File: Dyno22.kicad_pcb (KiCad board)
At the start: 2 copper layers, 52 parts, among them J1 Pwr Input, J2 Display, J3 Pwr Output, J4 BPM & Sensors, J7 UART, SW1 SW_DPST_x2, U1 TS2937CW50, U2 LM324, U3 74HC4052

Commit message: made some passive components 0805 and changed some routing
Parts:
- added TP5: GND_TestPoint, TestPoint:TestPoint_Loop_D2.60mm_Drill1.4mm_Beaded, F.Cu at (158.8, 128.9)
- D1: value Red -> Red LED
- D2: value LED -> RED LED; footprint LED_SMD:LED_0603_1608Metric -> LED_SMD:LED_0805_2012Metric
- Encoder1: footprint Rotary_Encoder:RotaryEncoder_Alps_EC11E_Vertical_H20mm -> Rotary_Encoder:RotaryEncoder_Alps_EC12E-Switch_Vertical_H20mm_CircularMountingHoles
- R18: value 2.2k -> 1k; footprint Resistor_SMD:R_0402_1005Metric -> Resistor_SMD:R_0805_2012Metric
- R3, R4, R5: value 5kΩ -> 4.7kΩ
- moved TP4 80.0 mm to (124.5, 35.6)
- moved D1 4.02 mm to (188.0, 47.9)
- moved D2 3.49 mm to (191.1, 47.9)
- moved R18 3.02 mm to (194.7, 48.3), turned to 0 degrees
- moved F1 2.54 mm to (200.7, 49.5), turned to 180 degrees
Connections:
- A1 pad 20: /MISO_0 -> /MOSI_1
- F1 pad 1: +24V -> Net-(J1-Pin_2)
- J1 pad 2: +24V -> Net-(J1-Pin_2)
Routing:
- net Net-(D2-K): track 3.34 -> 69.1 mm
- net +24V: track 74.9 -> 12.0 mm
- net Earth: track 41.4 -> 99.1 mm, vias 2 -> 3
- net /ROT_EN_SW: track 47.4 -> 79.8 mm, vias 1 -> 2
- net Net-(D2-A): track 11.3 -> 17.5 mm
- net Net-(D1-A): track 18.1 -> 22.5 mm
- net /BPM_CTRL_OUT: track 68.0 -> 71.3 mm
- net /KILL_SW: track 54.8 -> 53.8 mm
- net /FORCE_IN: track 29.0 -> 29.8 mm

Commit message: Added demux changed LED location changed some Rs
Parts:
- added U3: Demux, KiCADv6:SOIC-16WB_ONS, F.Cu at (173.0, 102.2)
- R3, R4, R5: value 4.7kΩ -> 10kΩ
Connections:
- D2 pad 1: Net-(D2-K) -> Earth
- F1 pad 2: Net-(D2-A) -> Net-(SW1-B)
- R18 pad 1: Net-(D2-K) -> +24V
- R18 pad 2: Earth -> Net-(D2-A)
- SW1 pad 2: Net-(D2-A) -> Net-(SW1-B)
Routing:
- net Net-(D2-K): track 69.1 -> 0.00 mm
- net (no net): track 0.00 -> 69.1 mm

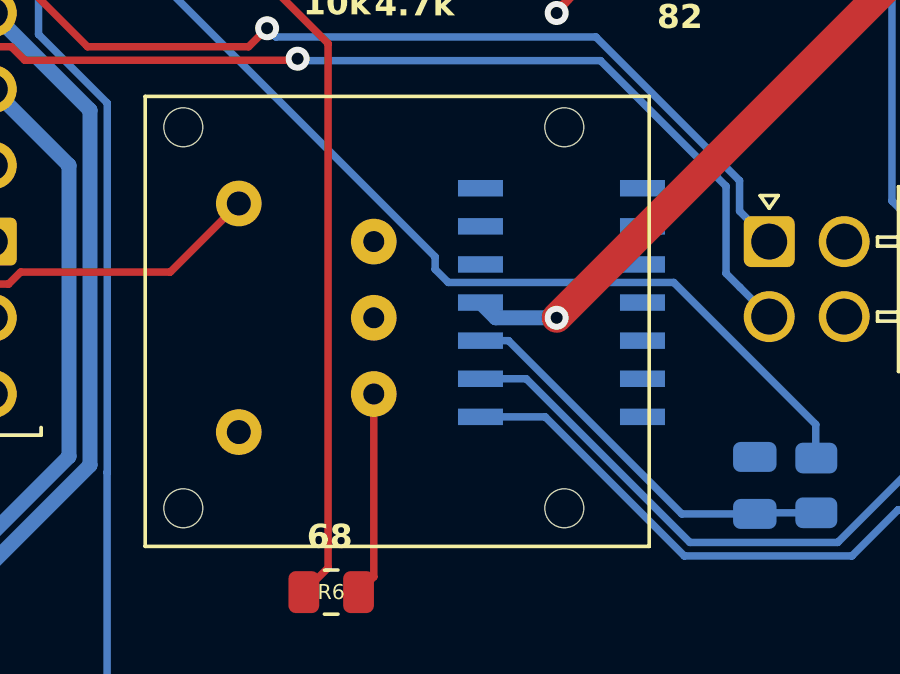
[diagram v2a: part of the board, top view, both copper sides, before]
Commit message: Amplifier footprint changes
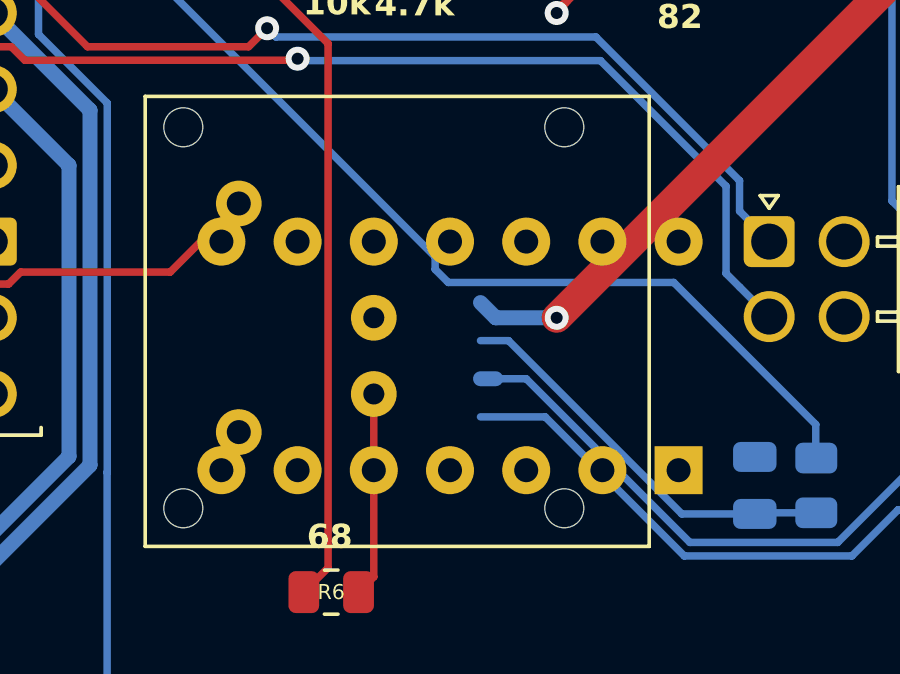
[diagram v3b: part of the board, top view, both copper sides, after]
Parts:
- U2: footprint SOIC:SOIC-14_W3.9mm -> Package_DIP:DIP-14_W7.62mm
- moved U2 6.82 mm to (205.7, 86.4)
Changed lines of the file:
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@@
     )
   )
-  (footprint "SOIC:SOIC-14_W3.9mm" (layer "B.Cu")
-    (at 201.836 80.772 90)
+  (footprint "Package_DIP:DIP-14_W7.62mm" (layer "B.Cu")
+    (at 205.74 86.36 90)
+    (descr "14-lead though-hole mounted DIP package, row spacing 7.62 mm (300 mils)")
+    (tags "THT DIP DIL PDIP 2.54mm 7.62mm 300mil")
     (property "Sheetfile" "Dyno22.kicad_sch")
     (property "Sheetname" "")
     (property "ki_description" "Low Power Single Operational Amplifier, SOT-23-5")
     (property "ki_keywords" "single opamp")
-    (attr smd)
-    (fp_text reference "U2" (at -5.715 0.16) (layer "B.SilkS")
+    (attr through_hole)
+    (fp_text reference "U2" (at 3.81 2.33 270) (layer "B.SilkS")
         (effects (font (size 1 1) (thickness 0.15)) (justify mirror))
     )
-    (fp_text value "LM324" (at 0 -5.29 90) (layer "B.Fab")
+    (fp_text value "LM324" (at 3.81 -17.57 270) (layer "B.Fab")
         (effects (font (size 1 1) (thickness 0.15)) (justify mirror))
     )
-    (fp_text user "REF**" (at 0 0 90) (layer "B.Fab")
+    (fp_text user "${REFERENCE}" (at 3.81 -7.62 270) (layer "B.Fab")
         (effects (font (size 1 1) (thickness 0.15)) (justify mirror))
     )
-    (fp_line (start -4.7 -2.3) (end -4.3 -2.3)
-      (stroke (width 0.1) (type solid)) (layer "B.SilkS"))
-    (fp_line (start -4.7 -1.7) (end -4.7 -2.3)
-      (stroke (width 0.1) (type solid)) (layer "B.SilkS"))
-    (fp_line (start -4.7 2.3) (end -4.7 1.9)
-      (stroke (width 0.1) (type solid)) (layer "B.SilkS"))
-    (fp_line (start -4.3 -2.3) (end -4.3 -3.2)
-      (stroke (width 0.1) (type solid)) (layer "B.SilkS"))
-    (fp_line (start -4.3 2.3) (end -4.7 2.3)
-      (stroke (width 0.1) (type solid)) (layer "B.SilkS"))
-    (fp_line (start 4.3 -2.3) (end 4.6 -2.3)
-      (stroke (width 0.1) (type solid)) (layer "B.SilkS"))
-    (fp_line (start 4.3 2.4) (end 4.7 2.4)
-      (stroke (width 0.1) (type solid)) (layer "B.SilkS"))
-    (fp_line (start 4.6 -2.3) (end 4.6 -1.9)
-      (stroke (width 0.1) (type solid)) (layer "B.SilkS"))
-    (fp_line (start 4.7 2.4) (end 4.7 1.9)
-      (stroke (width 0.1) (type solid)) (layer "B.SilkS"))
-    (fp_line (start -4.65 -3.7) (end -4.65 3.7)
+    (fp_line (start 1.16 -16.57) (end 6.46 -16.57)
+      (stroke (width 0.12) (type solid)) (layer "B.SilkS"))
+    (fp_line (start 1.16 1.33) (end 1.16 -16.57)
+      (stroke (width 0.12) (type solid)) (layer "B.SilkS"))
+    (fp_line (start 2.81 1.33) (end 1.16 1.33)
+      (stroke (width 0.12) (type solid)) (layer "B.SilkS"))
+    (fp_line (start 6.46 -16.57) (end 6.46 1.33)
+      (stroke (width 0.12) (type solid)) (layer "B.SilkS"))
+    (fp_line (start 6.46 1.33) (end 4.81 1.33)
+      (stroke (width 0.12) (type solid)) (layer "B.SilkS"))
+    (fp_arc (start 2.81 1.33) (mid 3.81 0.33) (end 4.81 1.33)
+      (stroke (width 0.12) (type solid)) (layer "B.SilkS"))
+    (fp_line (start -1.1 -16.8) (end 8.7 -16.8)
       (stroke (width 0.05) (type solid)) (layer "B.CrtYd"))
-    (fp_line (start -4.65 -3.7) (end 4.65 -3.7)
+    (fp_line (start -1.1 1.55) (end -1.1 -16.8)
       (stroke (width 0.05) (type solid)) (layer "B.CrtYd"))
-    (fp_line (start 4.65 3.7) (end -4.65 3.7)
+    (fp_line (start 8.7 -16.8) (end 8.7 1.55)
       (stroke (width 0.05) (type solid)) (layer "B.CrtYd"))
-    (fp_line (start 4.65 3.7) (end 4.65 -3.7)
+    (fp_line (start 8.7 1.55) (end -1.1 1.55)
       (stroke (width 0.05) (type solid)) (layer "B.CrtYd"))
-    (fp_line (start -4.4 -2) (end 4.4 -2)
+    (fp_line (start 0.635 -16.51) (end 0.635 0.27)
       (stroke (width 0.1) (type solid)) (layer "B.Fab"))
-    (fp_line (start -4.4 2) (end -4.4 -2)
+    (fp_line (start 0.635 0.27) (end 1.635 1.27)
       (stroke (width 0.1) (type solid)) (layer "B.Fab"))
-    (fp_line (start -4.4 2) (end 4.4 2)
+    (fp_line (start 1.635 1.27) (end 6.985 1.27)
       (stroke (width 0.1) (type solid)) (layer "B.Fab"))
-    (fp_line (start 4.4 2) (end 4.4 -2)
+    (fp_line (start 6.985 -16.51) (end 0.635 -16.51)
       (stroke (width 0.1) (type solid)) (layer "B.Fab"))
-    (pad "1" smd rect (at -3.81 -2.7 90) (size 0.55 1.5) (layers "B.Cu" "B.Paste" "B.Mask")
-      (net 31 "/BPM_CTRL") (pintype "output") (solder_mask_margin 0.07))
-    (pad "2" smd rect (at -2.54 -2.7 90) (size 0.55 1.5) (layers "B.Cu" "B.Paste" "B.Mask")
-      (net 42 "Net-(U2--)") (pinfunction "-") (pintype "input") (solder_mask_margin 0.07))
-    (pad "3" smd rect (at -1.27 -2.7 90) (size 0.55 1.5) (layers "B.Cu" "B.Paste" "B.Mask")
-      (net 30 "Net-(U2-+)") (pinfunction "+") (pintype "input") (solder_mask_margin 0.07))
-    (pad "4" smd rect (at 0 -2.7 90) (size 0.55 1.5) (layers "B.Cu" "B.Paste" "B.Mask")
-      (net 29 "+24V") (pinfunction "V+") (pintype "power_in") (solder_mask_margin 0.07))
-    (pad "5" smd rect (at 1.27 -2.7 90) (size 0.55 1.5) (layers "B.Cu" "B.Paste" "B.Mask")
-      (solder_mask_margin 0.07))
-    (pad "6" smd rect (at 2.54 -2.7 90) (size 0.55 1.5) (layers "B.Cu" "B.Paste" "B.Mask")
-      (solder_mask_margin 0.07))
-    (pad "7" smd rect (at 3.81 -2.7 90) (size 0.55 1.5) (layers "B.Cu" "B.Paste" "B.Mask")
-      (solder_mask_margin 0.07))
-    (pad "8" smd rect (at 3.81 2.7 90) (size 0.55 1.5) (layers "B.Cu" "B.Paste" "B.Mask")
-      (solder_mask_margin 0.07))
-    (pad "9" smd rect (at 2.54 2.7 90) (size 0.55 1.5) (layers "B.Cu" "B.Paste" "B.Mask")
-      (solder_mask_margin 0.07))
-    (pad "10" smd rect (at 1.27 2.7 90) (size 0.55 1.5) (layers "B.Cu" "B.Paste" "B.Mask")
-      (solder_mask_margin 0.07))
-    (pad "11" smd rect (at 0 2.7 90) (size 0.55 1.5) (layers "B.Cu" "B.Paste" "B.Mask")
-      (net 4 "Earth") (pinfunction "V-") (pintype "power_in") (solder_mask_margin 0.07))
-    (pad "12" smd rect (at -1.27 2.7 90) (size 0.55 1.5) (layers "B.Cu" "B.Paste" "B.Mask")
-      (solder_mask_margin 0.07))
-    (pad "13" smd rect (at -2.54 2.7 90) (size 0.55 1.5) (layers "B.Cu" "B.Paste" "B.Mask")
-      (solder_mask_margin 0.07))
-    (pad "14" smd rect (at -3.81 2.7 90) (size 0.55 1.5) (layers "B.Cu" "B.Paste" "B.Mask")
-      (solder_mask_margin 0.07))
+    (fp_line (start 6.985 1.27) (end 6.985 -16.51)
+      (stroke (width 0.1) (type solid)) (layer "B.Fab"))
+    (pad "1" thru_hole rect (at 0 0 90) (size 1.6 1.6) (drill 0.8) (layers "*.Cu" "*.Mask")
+      (net 31 "/BPM_CTRL") (pintype "output"))
+    (pad "2" thru_hole oval (at 0 -2.54 90) (size 1.6 1.6) (drill 0.8) (layers "*.Cu" "*.Mask")
+      (net 42 "Net-(U2--)") (pinfunction "-") (pintype "input"))
+    (pad "3" thru_hole oval (at 0 -5.08 90) (size 1.6 1.6) (drill 0.8) (layers "*.Cu" "*.Mask")
+      (net 30 "Net-(U2-+)") (pinfunction "+") (pintype "input"))
+    (pad "4" thru_hole oval (at 0 -7.62 90) (size 1.6 1.6) (drill 0.8) (layers "*.Cu" "*.Mask")
+      (net 29 "+24V") (pinfunction "V+") (pintype "power_in"))
+    (pad "5" thru_hole oval (at 0 -10.16 90) (size 1.6 1.6) (drill 0.8) (layers "*.Cu" "*.Mask"))
+    (pad "6" thru_hole oval (at 0 -12.7 90) (size 1.6 1.6) (drill 0.8) (layers "*.Cu" "*.Mask"))
+    (pad "7" thru_hole oval (at 0 -15.24 90) (size 1.6 1.6) (drill 0.8) (layers "*.Cu" "*.Mask"))
+    (pad "8" thru_hole oval (at 7.62 -15.24 90) (size 1.6 1.6) (drill 0.8) (layers "*.Cu" "*.Mask"))
+    (pad "9" thru_hole oval (at 7.62 -12.7 90) (size 1.6 1.6) (drill 0.8) (layers "*.Cu" "*.Mask"))
+    (pad "10" thru_hole oval (at 7.62 -10.16 90) (size 1.6 1.6) (drill 0.8) (layers "*.Cu" "*.Mask"))
+    (pad "11" thru_hole oval (at 7.62 -7.62 90) (size 1.6 1.6) (drill 0.8) (layers "*.Cu" "*.Mask")
+      (net 4 "Earth") (pinfunction "V-") (pintype "power_in"))
+    (pad "12" thru_hole oval (at 7.62 -5.08 90) (size 1.6 1.6) (drill 0.8) (layers "*.Cu" "*.Mask"))
+    (pad "13" thru_hole oval (at 7.62 -2.54 90) (size 1.6 1.6) (drill 0.8) (layers "*.Cu" "*.Mask"))
+    (pad "14" thru_hole oval (at 7.62 0 90) (size 1.6 1.6) (drill 0.8) (layers "*.Cu" "*.Mask"))
+    (model "${KICAD6_3DMODEL_DIR}/Package_DIP.3dshapes/DIP-14_W7.62mm.wrl"
+      (offset (xyz 0 0 0))
+      (scale (xyz 1 1 1))
+      (rotate (xyz 0 0 0))
+    )
   )
   (footprint "Capacitor_SMD:C_1206_3216Metric" (layer "B.Cu")

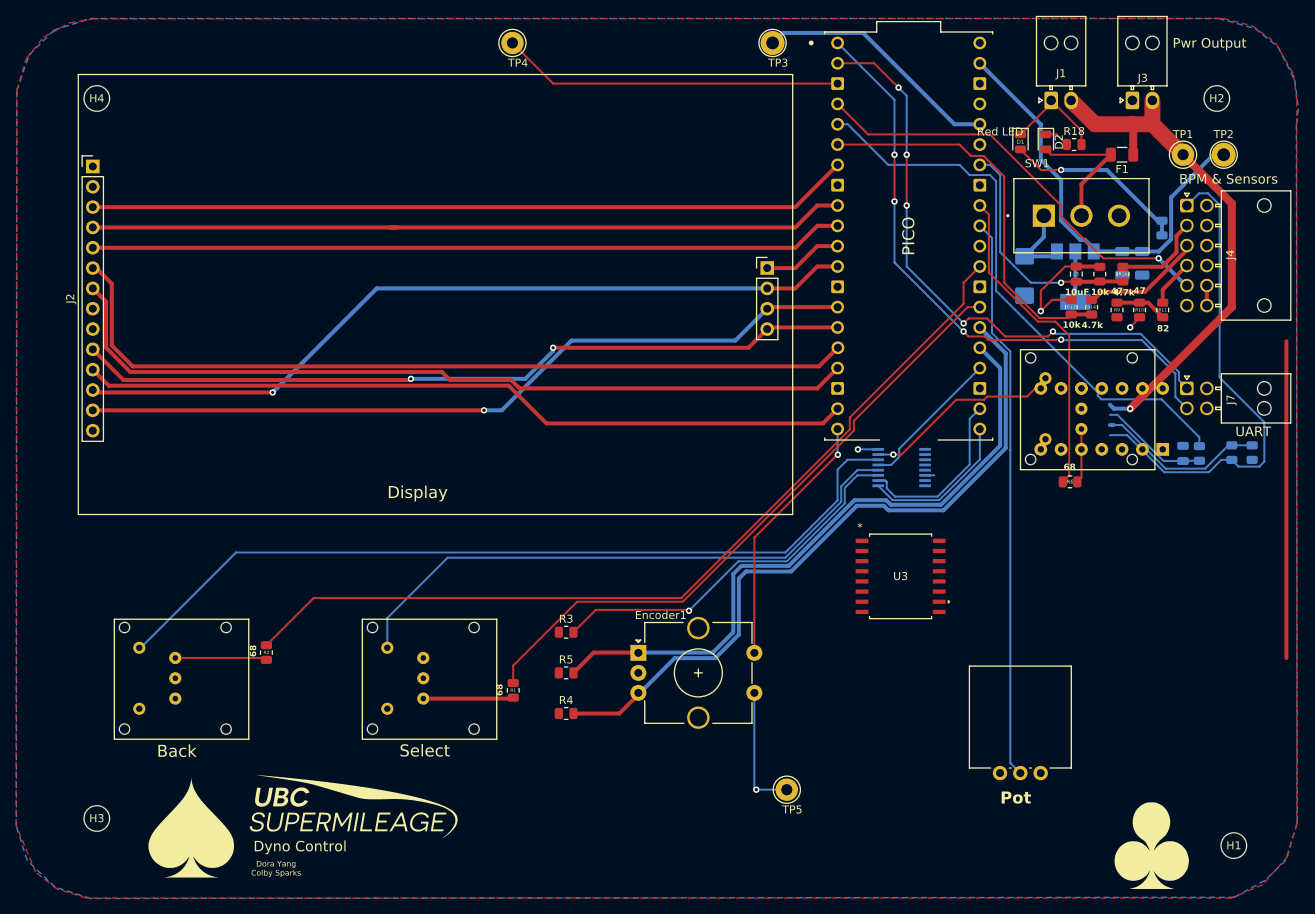
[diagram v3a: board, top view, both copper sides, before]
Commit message: Changed routing and component placement AGAIN
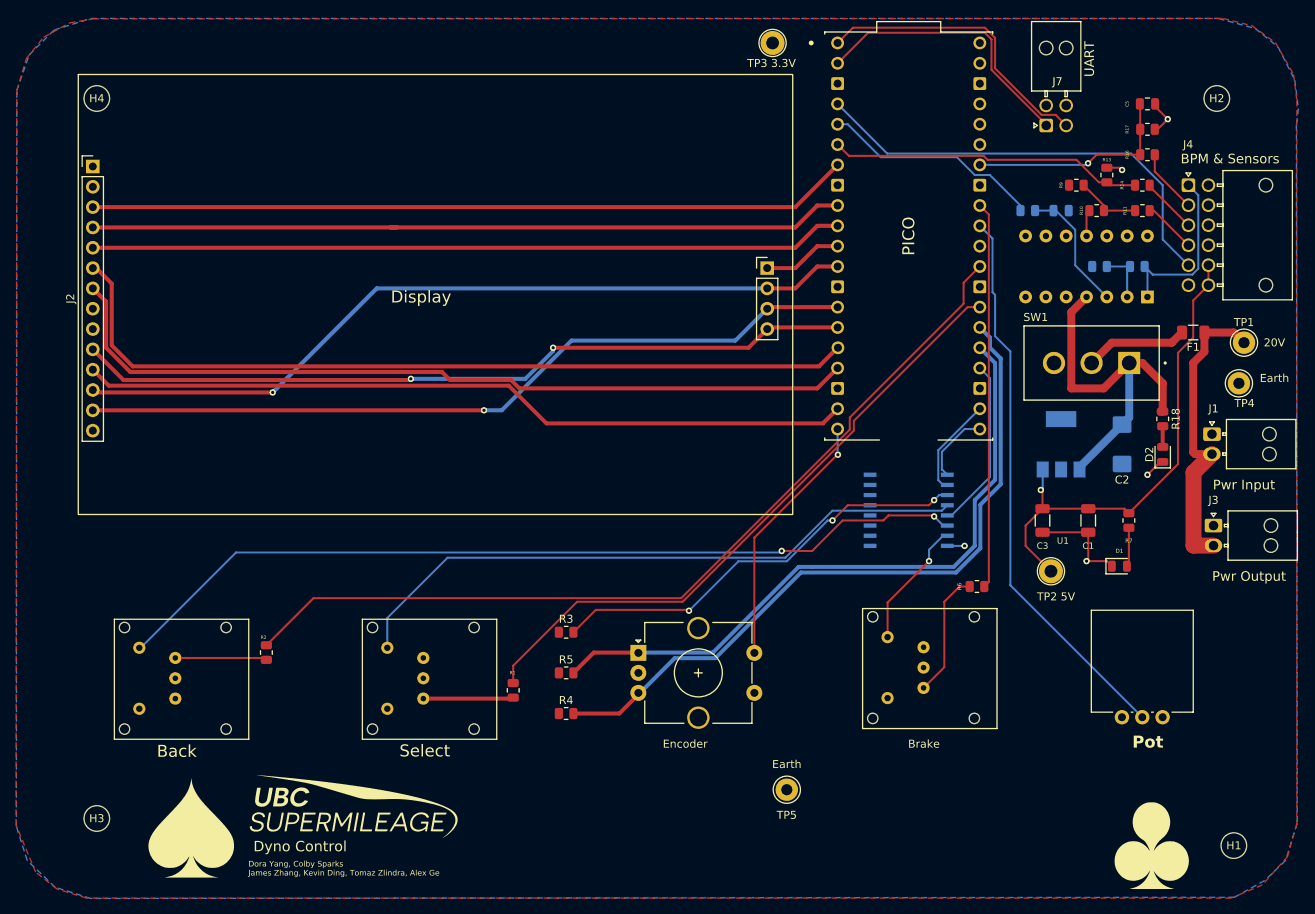
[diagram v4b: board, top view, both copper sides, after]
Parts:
- removed the U3 at (173.1, 88.6)
- C1, C3, R7: moved to F.Cu
- TP2 5V: renamed from TP2
- TP3 3.3V: renamed from TP3
- U3: moved to B.Cu
- moved TP4 100.3 mm to (215.3, 78.1)
- moved TP2 5V 56.4 mm to (191.8, 101.6)
- moved D1 54.5 mm to (200.3, 101.0), turned to 0 degrees
- moved J3 54.1 mm to (212.1, 95.9), turned to 0 degrees
- moved J1 46.3 mm to (211.9, 84.5), turned to 0 degrees
- moved D2 41.7 mm to (205.7, 87.0), turned to 90 degrees
- moved S3 37.9 mm to (168.2, 106.3)
- moved J7 37.3 mm to (191.2, 45.9), turned to 90 degrees
- moved R8 37.2 mm to (188.9, 56.5), turned to 180 degrees
- moved R7 36.8 mm to (201.5, 95.2), turned to 90 degrees
- moved R18 36.0 mm to (205.7, 82.5), turned to -90 degrees
- moved C4 34.0 mm to (193.0, 56.5), turned to 0 degrees
- moved C3 33.7 mm to (190.7, 95.2)
- moved C1 32.8 mm to (196.4, 95.2)
- moved R12 30.1 mm to (197.8, 63.5), turned to 180 degrees
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- renumbered Encoder1 to Encoder
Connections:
- F1 pad 1: Net-(J1-Pin_2) -> +24V
- J1 pad 2: Net-(J1-Pin_2) -> +24V
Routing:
- net Earth: track 99.1 -> 26.3 mm, vias 3 -> 4
- net +24V: track 12.0 -> 84.1 mm, vias 1 -> 0
- net (no net): track 69.1 -> 0.00 mm
- net /BPM_CTRL_OUT: track 71.3 -> 28.2 mm
- net /UART_RX: track 75.3 -> 34.8 mm, vias 5 -> 0
- net /UART_TX: track 76.2 -> 36.7 mm, vias 4 -> 0
- net /BPM_CTRL: track 62.2 -> 22.7 mm
- net +3.3V: track 33.7 -> 2.16 mm
- net Net-(S3-L1_Y): track 46.4 -> 15.8 mm
- net Net-(D1-A): track 22.5 -> 4.85 mm, vias 1 -> 0
- net Net-(D2-A): track 17.5 -> 2.59 mm
- net Net-(U2--): track 21.2 -> 6.86 mm
- net Net-(SW1-B): track 0.00 -> 12.9 mm
- net /DEMUX_S1: track 19.4 -> 9.14 mm
- net /OP_IN: track 48.7 -> 39.3 mm
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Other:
- board text added: "20V"
- board text added: "Brake"
- board text added: "Dora Yang, Colby Sparks James Zhang, Kevin Ding, Tomaz Zlindra, Alex Ge"
- board text added: "Earth"
- board text added: "Pwr Input"
- board text added: "R17"
- board text removed: "Dora Yang Colby Sparks"

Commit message: Forgot to save schematic changes
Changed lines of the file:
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@@
   (segment (start 200.94869 93.775) (end 201.51119 94.3375) (width 0.25) (layer "F.Cu") (net 27))
   (segment (start 196.43119 93.775) (end 200.94869 93.775) (width 0.25) (layer "F.Cu") (net 27))
+  (segment (start 190.5 91.44) (end 190.71619 91.65619) (width 0.25) (layer "F.Cu") (net 27))
   (segment (start 211.455 63.34) (end 211.455 65.84) (width 0.25) (layer "F.Cu") (net 27))
   (segment (start 207.645 74.295) (end 209.55 72.39) (width 0.25) (layer "F.Cu") (net 27))
@@
   (segment (start 190.71619 93.775) (end 196.43119 93.775) (width 0.25) (layer "F.Cu") (net 27))
   (segment (start 188.595 98.425) (end 191.77 101.6) (width 0.25) (layer "F.Cu") (net 27))
-  (segment (start 190.71619 93.775) (end 190.71619 91.65619) (width 0.25) (layer "F.Cu") (net 27))
   (segment (start 209.55 67.745) (end 211.455 65.84) (width 0.25) (layer "F.Cu") (net 27))
-  (segment (start 190.71619 91.65619) (end 190.5 91.44) (width 0.25) (layer "F.Cu") (net 27))
+  (segment (start 190.71619 91.65619) (end 190.71619 93.775) (width 0.25) (layer "F.Cu") (net 27))
   (segment (start 209.55 72.39) (end 209.55 67.745) (width 0.25) (layer "F.Cu") (net 27))
   (segment (start 190.71619 93.775) (end 188.595 95.89619) (width 0.25) (layer "F.Cu") (net 27))
@@
   (segment (start 201.51119 94.3375) (end 207.645 88.20369) (width 0.25) (layer "F.Cu") (net 27))
   (via (at 190.5 91.44) (size 0.8) (drill 0.4) (layers "F.Cu" "B.Cu") (free) (net 27))
-  (segment (start 190.74 88.875) (end 190.74 91.2) (width 0.25) (layer "B.Cu") (net 27))
-  (segment (start 190.74 91.2) (end 190.5 91.44) (width 0.25) (layer "B.Cu") (net 27))
+  (segment (start 190.74 91.2) (end 190.74 88.875) (width 0.25) (layer "B.Cu") (net 27))
+  (segment (start 190.5 91.44) (end 190.74 91.2) (width 0.25) (layer "B.Cu") (net 27))
   (segment (start 209.55 86.71) (end 209.55 75.565) (width 1) (layer "F.Cu") (net 29))
   (segment (start 201.55 75.565) (end 203.2 75.565) (width 1) (layer "F.Cu") (net 29))

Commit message: Fix the earth, the earth is our home
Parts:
- TP2: renamed from TP2 5V
- TP3: renamed from TP3 3.3V
- moved TP2 36.2 mm to (191.1, 137.8)
- moved TP5 25.7 mm to (182.9, 137.8)
- moved J3 11.4 mm to (211.9, 84.5)
- moved J1 10.8 mm to (211.9, 95.3)
- moved TP4 3.81 mm to (219.1, 78.1)
- moved TP1 3.24 mm to (219.1, 72.4)
- renumbered Encoder to Encoder1
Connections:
- A1 pad 20: /MOSI_1 -> /ROT_EN_SW
- F1 pad 1: +24V -> /20V_IN
- J1 pad 2: +24V -> /20V_IN
- TP1 pad 1: +24V -> /20V_IN
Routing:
- net +5V: track 61.3 -> 161.5 mm
- net /20V_IN: track 0.00 -> 36.6 mm
- net /KILL_SW: track 56.2 -> 84.8 mm
- net +24V: track 84.1 -> 64.1 mm
- net /BTN_BRAKE: track 16.1 -> 17.9 mm
- net /LED_BRAKE: track 48.3 -> 49.6 mm
- net /BPM_CTRL_OUT: track 28.2 -> 28.9 mm
- net +3.3V: track 2.16 -> 1.65 mm
- net /OP_IN: track 39.3 -> 39.5 mm, vias 0 -> 1
